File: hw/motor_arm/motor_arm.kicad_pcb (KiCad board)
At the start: 2 copper layers, 32.4 x 16 mm, 52 parts, among them J1 Conn_01x05, U1 AP7370-33W5-7, U10 RF4E110GN, U11 RF4E110GN, U2 IR2101, U3 RF4E110GN, U4 RF4E110GN, U5 IR2101, U6 RF4E110GN, U7 EFM8BB21F16I-C-QFN20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

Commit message: created test pcb
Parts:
- added U12: MIC4604YMT, Custom:MIC4604-TDFN2525-10, F.Cu at (55.3, 78.3)
- added U13: MIC4604YMT, Custom:MIC4604-TDFN2525-10, F.Cu at (75.4, 78.3)
- added U14: MIC4604YMT, Custom:MIC4604-TDFN2525-10, F.Cu at (96.3, 78.3)
- C1, C2, C3, C4, C5, C6, C7, C8, C9: footprint Capacitor_SMD:C_0805_2012Metric_Pad1.15x1.40mm_HandSolder -> Capacitor_SMD:C_0603_1608Metric_Pad1.05x0.95mm_HandSolder
- R1, R10, R11, R12, R13, R14, R15, R16, R17, R2, R3, R4, R5, R6, R7, R8, R9: footprint Resistor_SMD:R_0805_2012Metric_Pad1.15x1.40mm_HandSolder -> Resistor_SMD:R_0603_1608Metric_Pad1.05x0.95mm_HandSolder
- moved H6 123.0 mm to (48.3, 60.6)
- moved U4 111.3 mm to (45.0, 80.2)
- moved R1 108.3 mm to (48.7, 84.2)
- moved C4 105.3 mm to (48.6, 87.6), turned to 180 degrees
- moved R17 102.8 mm to (53.7, 66.2)
- moved U6 102.6 mm to (65.3, 85.3)
- moved R5 102.4 mm to (48.7, 80.9)
- moved C3 102.1 mm to (61.2, 83.5), turned to 90 degrees
- moved H7 95.8 mm to (56.0, 91.8), turned to 90 degrees
- moved U8 95.8 mm to (65.4, 80.2)
- moved U1 93.2 mm to (67.6, 66.4)
- moved R12 92.0 mm to (72.8, 67.3), turned to 90 degrees
- moved H2 90.8 mm to (71.1, 91.8), turned to 90 degrees
- moved H1 90.2 mm to (51.0, 91.8), turned to 90 degrees
- moved TP1 89.9 mm to (69.2, 73.4)
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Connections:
- U1 pad 4: Net-(U1-Pad3) -> Net-(U1-Pad4)
- U7 pad 19: VirtualGnd -> Net-(U7-Pad19)
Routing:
- net PhaseA: track 0.00 -> 133.8 mm, vias 0 -> 4
- net PhaseB: track 0.00 -> 108.8 mm, vias 0 -> 4
- net PhaseC: track 0.00 -> 74.3 mm, vias 0 -> 4
- net CH: track 0.00 -> 57.5 mm, vias 0 -> 6
- net GND: track 0.00 -> 52.9 mm, vias 0 -> 19
- net vdC: track 0.00 -> 49.6 mm, vias 0 -> 4
- net AH: track 0.00 -> 47.9 mm, vias 0 -> 4
- net AL: track 0.00 -> 45.2 mm, vias 0 -> 4
- net CL: track 0.00 -> 42.4 mm, vias 0 -> 5
- net vdB: track 0.00 -> 41.4 mm, vias 0 -> 2
- net RX: track 0.00 -> 39.1 mm, vias 0 -> 4
- net vdA: track 0.00 -> 34.7 mm, vias 0 -> 2
- net TX: track 0.00 -> 33.0 mm, vias 0 -> 4
- net +3V3: track 0.00 -> 31.7 mm, vias 0 -> 4
- net BH: track 0.00 -> 28.5 mm, vias 0 -> 2
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- added copper zone on F.Cu, net +12V
- added copper zone on B.Cu, net GND
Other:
- board size 32.4 x 16 mm -> 62 x 39 mm
- board text added: "Micro Drone ESC Test PCB v1.0 U.Saini and K.Kurucz"

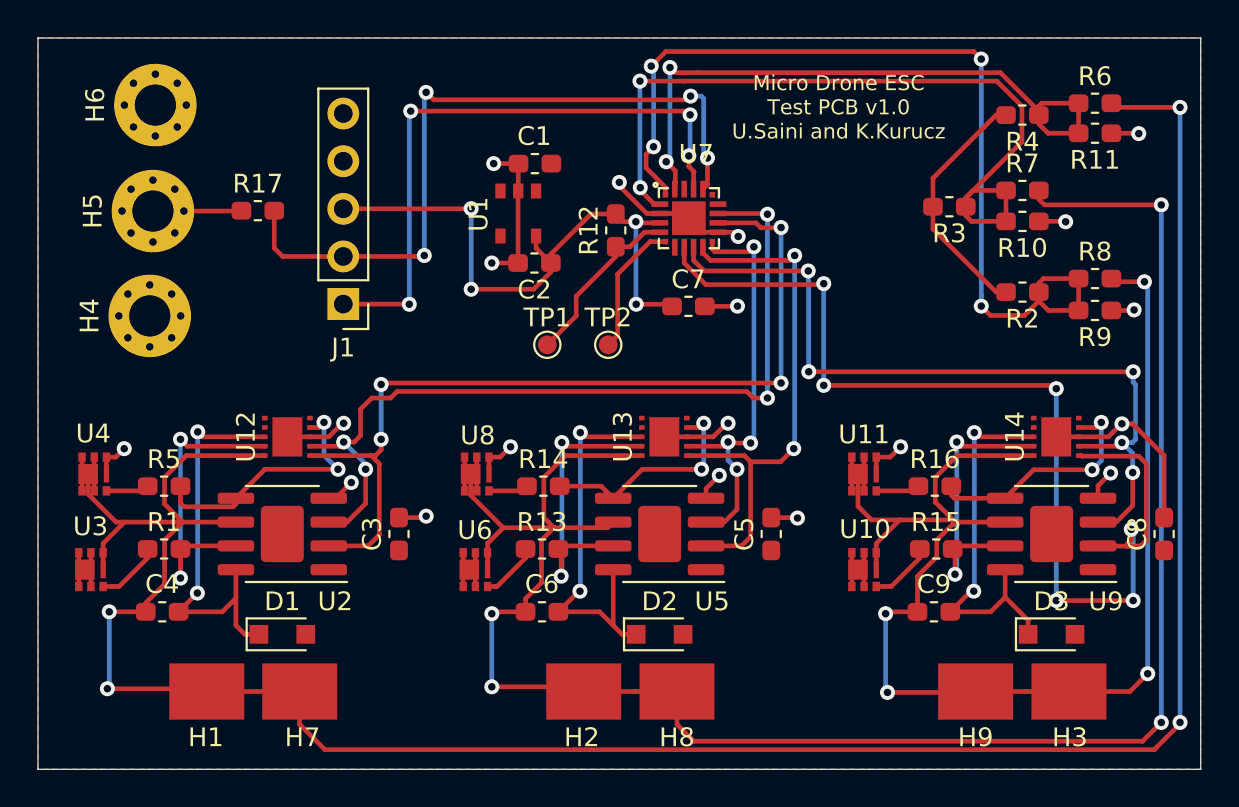
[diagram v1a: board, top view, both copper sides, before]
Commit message: modified top layer to have routed 12 V rather than cu pour
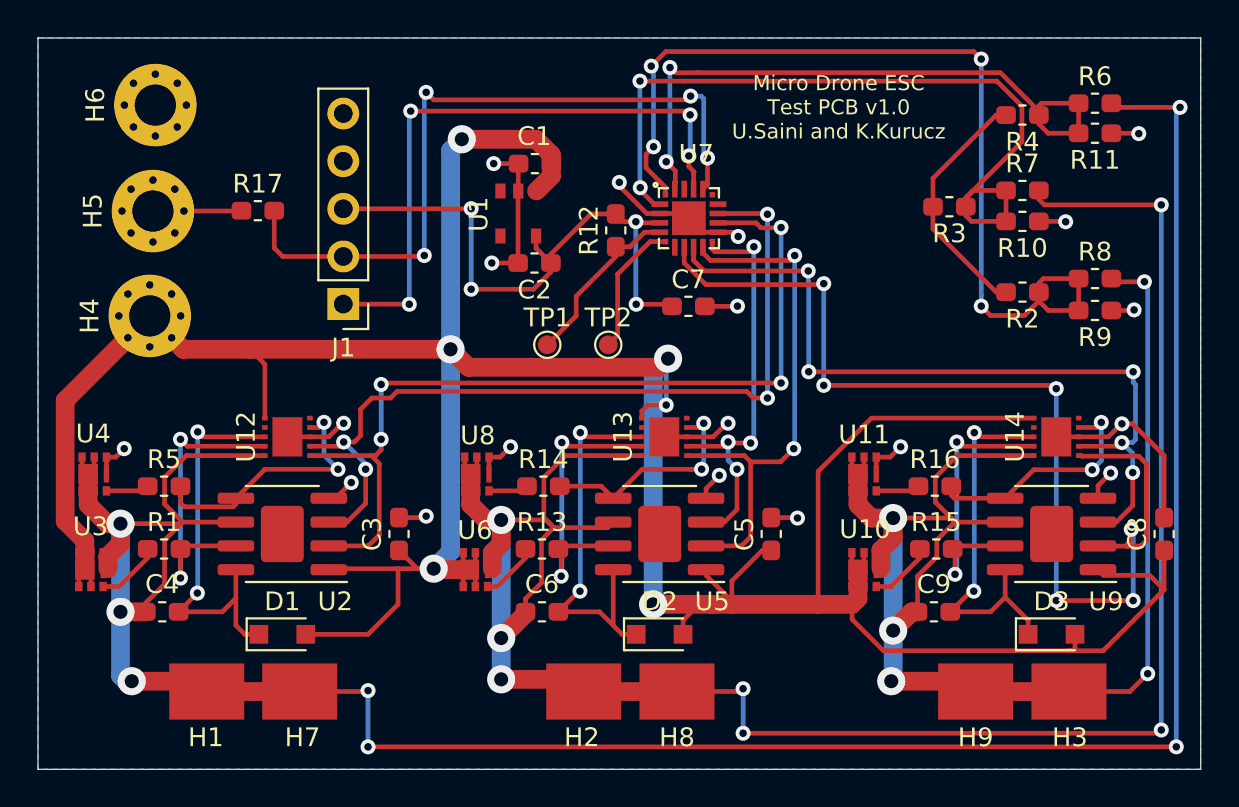
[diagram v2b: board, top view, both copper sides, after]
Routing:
- net +12V: track 12.4 -> 195.3 mm, vias 0 -> 6
- net PhaseB: track 108.8 -> 115.0 mm, vias 4 -> 7
- net PhaseA: track 133.8 -> 139.0 mm, vias 4 -> 7
- net PhaseC: track 74.3 -> 79.5 mm, vias 4 -> 5
- removed copper zone on F.Cu, net +12V

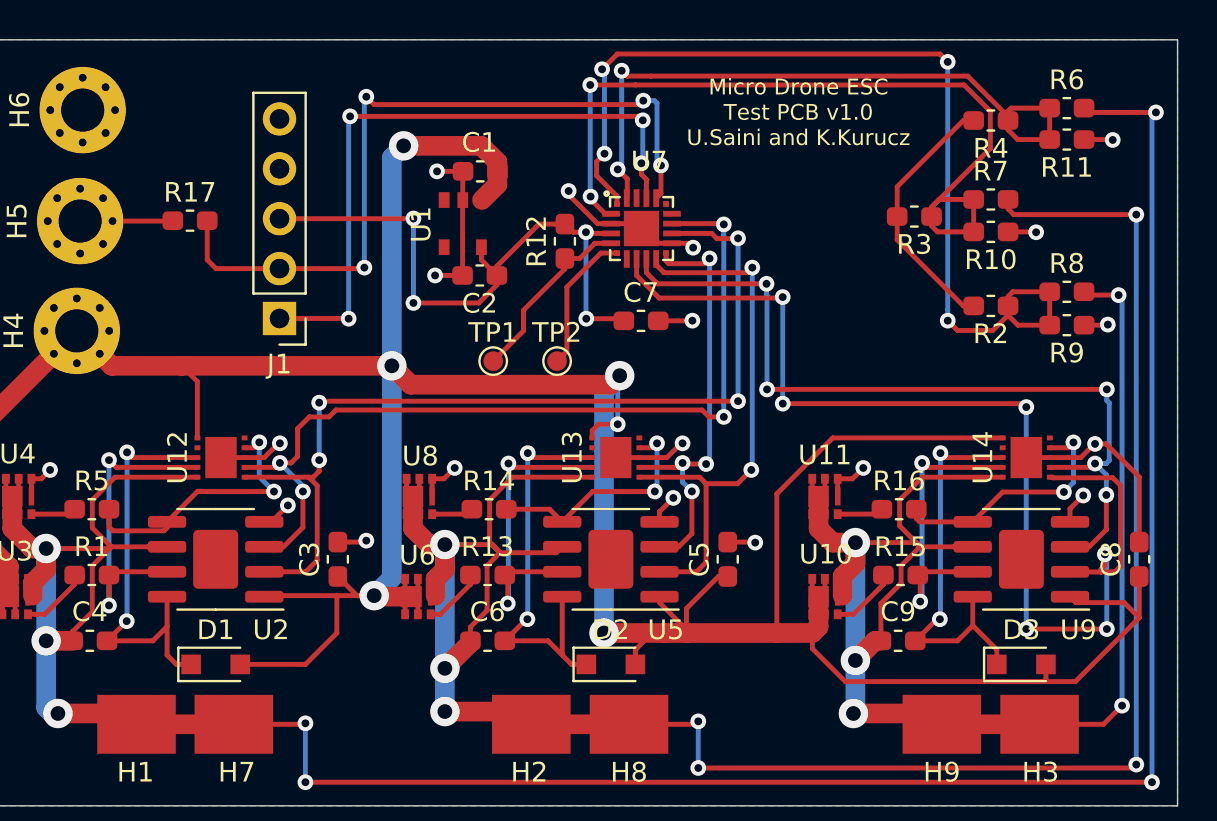
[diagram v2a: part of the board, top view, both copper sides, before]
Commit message: generated gerbers for esc v1
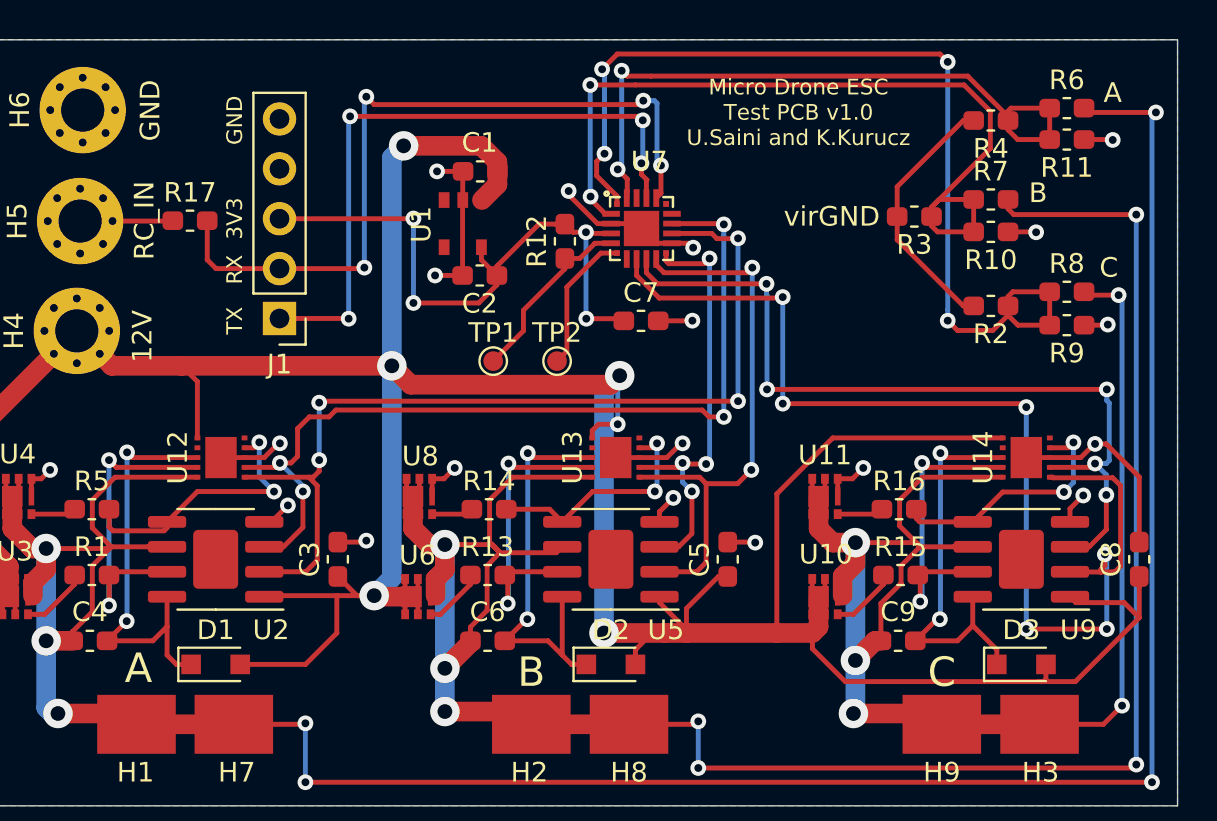
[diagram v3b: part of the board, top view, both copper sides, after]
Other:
- board text added: "12V"
- board text added: "3V3"
- board text added: "A"
- board text added: "B"
- board text added: "C"
- board text added: "GND"
- board text added: "RC_IN"
- board text added: "RX"
- board text added: "TX"
- board text added: "virGND"
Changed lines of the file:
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@@
   (general
     (thickness 1.6)
-    (drawings 5)
+    (drawings 19)
     (tracks 725)
     (zones 0)
@@
     (visible_elements 7FFFFFFF)
     (pcbplotparams
-      (layerselection 0x010fc_ffffffff)
-      (usegerberextensions false)
+      (layerselection 0x010f0_ffffffff)
+      (usegerberextensions true)
       (usegerberattributes false)
       (usegerberadvancedattributes false)
@@
       (psa4output false)
       (plotreference true)
-      (plotvalue true)
+      (plotvalue false)
       (plotinvisibletext false)
       (padsonsilk false)
@@
       (outputformat 1)
       (mirror false)
-      (drillshape 1)
+      (drillshape 0)
       (scaleselection 1)
-      (outputdirectory ""))
+      (outputdirectory "gerbers/"))
   )
   (net 0 "")
@@
     )
   )
+  (gr_text RC_IN (at 51.4 66.2 90) (layer F.SilkS)
+    (effects (font (size 1 1) (thickness 0.15)))
+  )
+  (gr_text 12V (at 51.3 72.1 90) (layer F.SilkS)
+    (effects (font (size 1 1) (thickness 0.15)))
+  )
+  (gr_text GND (at 51.7 60.6 90) (layer F.SilkS)
+    (effects (font (size 1 1) (thickness 0.15)))
+  )
+  (gr_text C (at 100.5 68.6) (layer F.SilkS)
+    (effects (font (size 1 1) (thickness 0.15)))
+  )
+  (gr_text B (at 96.9 64.8) (layer F.SilkS)
+    (effects (font (size 1 1) (thickness 0.15)))
+  )
+  (gr_text A (at 100.7 59.7) (layer F.SilkS)
+    (effects (font (size 1 1) (thickness 0.15)))
+  )
+  (gr_text virGND (at 86.4 66) (layer F.SilkS)
+    (effects (font (size 1 1) (thickness 0.15)))
+  )
+  (gr_text C (at 92 89.2) (layer F.SilkS)
+    (effects (font (size 1.5 1.5) (thickness 0.15)))
+  )
+  (gr_text B (at 71.1 89.2) (layer F.SilkS)
+    (effects (font (size 1.5 1.5) (thickness 0.15)))
+  )
+  (gr_text A (at 51.1 89) (layer F.SilkS)
+    (effects (font (size 1.5 1.5) (thickness 0.15)))
+  )
+  (gr_text 3V3 (at 56 66.1 90) (layer F.SilkS)
+    (effects (font (size 0.8 0.8) (thickness 0.15)))
+  )
+  (gr_text RX (at 56 68.7 90) (layer F.SilkS)
+    (effects (font (size 0.8 0.8) (thickness 0.15)))
+  )
+  (gr_text TX (at 56 71.3 90) (layer F.SilkS)
+    (effects (font (size 0.8 0.8) (thickness 0.15)))
+  )
+  (gr_text GND (at 56 61.1 90) (layer F.SilkS)
+    (effects (font (size 0.8 0.8) (thickness 0.15)))
+  )
   (gr_text "Micro Drone ESC\nTest PCB v1.0\nU.Saini and K.Kurucz" (at 84.7 60.7) (layer F.SilkS)
